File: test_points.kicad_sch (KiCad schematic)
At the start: 17 parts

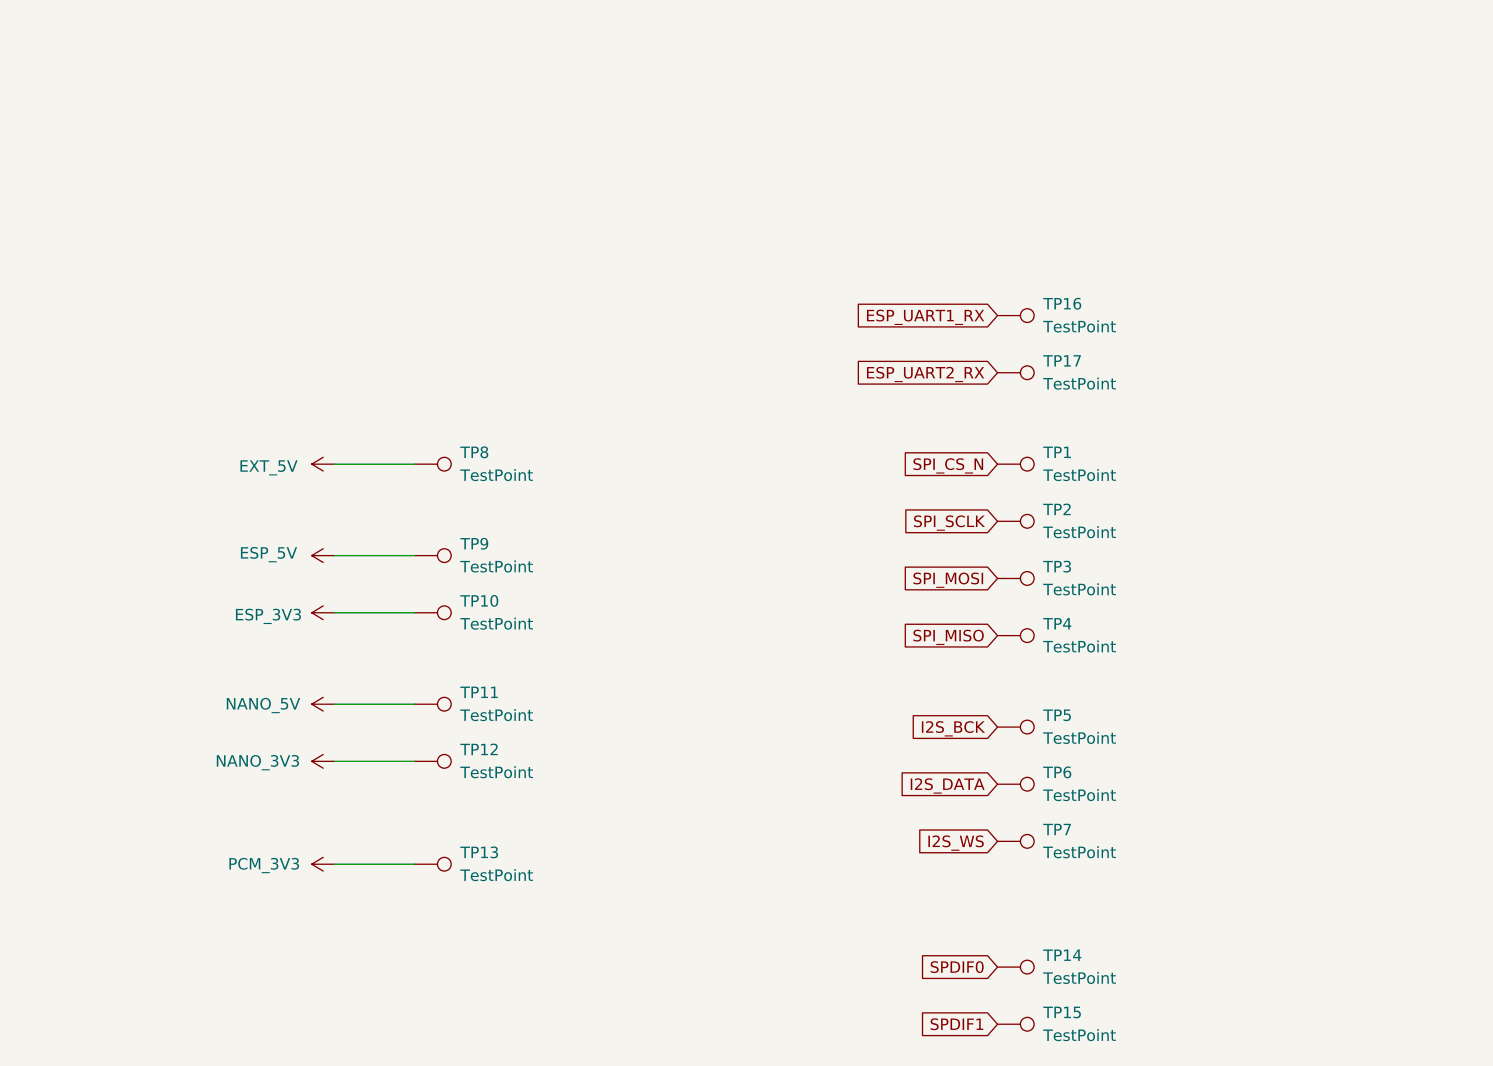
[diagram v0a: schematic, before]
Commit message: Added pin headers for SPI3, I2C0 and I2C1
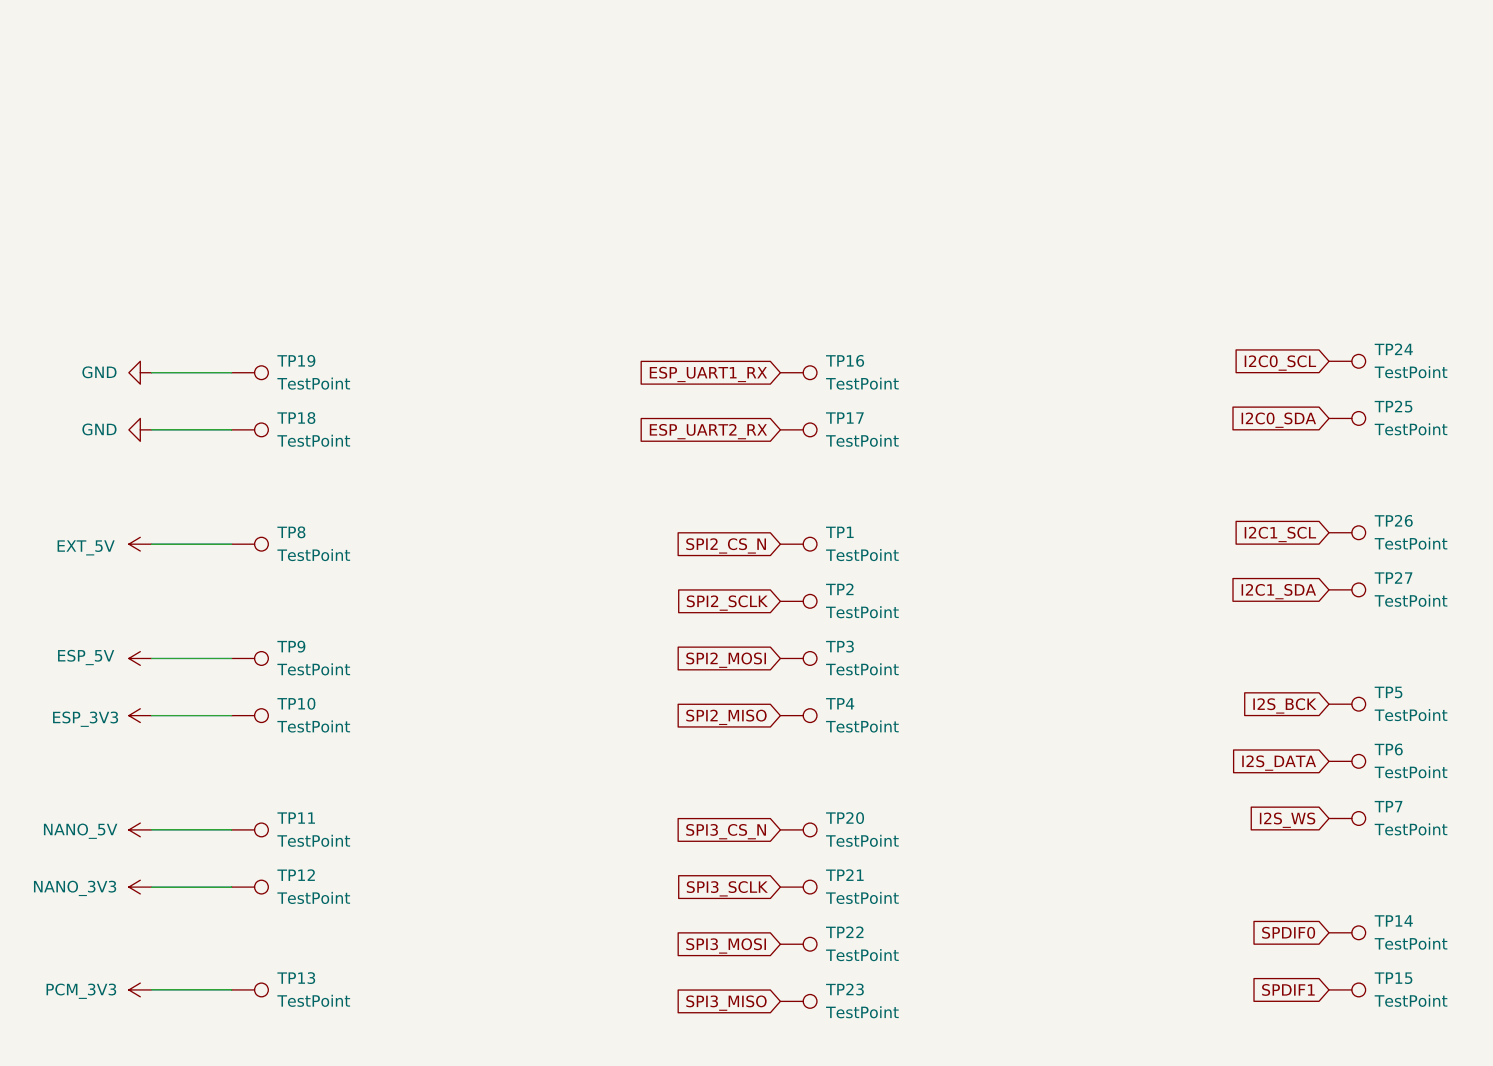
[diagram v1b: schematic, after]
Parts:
- added TP18, TP19, TP20, TP21, TP22, TP23, TP24, TP25, TP26, TP27: TestPoint, symbol Connector:TestPoint
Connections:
- net SPI_CS_N renamed SPI2_CS_N
- net SPI_MISO renamed SPI2_MISO
- net SPI_MOSI renamed SPI2_MOSI
- net SPI_SCLK renamed SPI2_SCLK
- new net GND: TP18.1, TP19.1
- new net I2C0_SCL: TP24.1
- new net I2C0_SDA: TP25.1
- new net I2C1_SCL: TP26.1
- new net I2C1_SDA: TP27.1
- new net SPI3_CS_N: TP20.1
- new net SPI3_MISO: TP23.1
- new net SPI3_MOSI: TP22.1
- new net SPI3_SCLK: TP21.1
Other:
- moved on the sheet: TP1, TP10, TP11, TP12, TP13, TP14, TP15, TP16, TP17, TP2, TP3, TP4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

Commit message: Added jumpers for FM and FIL to DAC. Added pin headers for audio out to DAC. Minor adjustments.
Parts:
- added TP28, TP29: TestPoint, TestPoint:TestPoint_Plated_Hole_D2.0mm, symbol Connector:TestPoint
- TP1, TP10, TP11, TP12, TP13, TP14, TP15, TP16, TP17, TP18, TP19, TP2, TP20, TP21, TP22, TP23, TP24, TP25, TP26, TP27, TP3, TP4, TP5, TP6, TP7, TP8, TP9: footprint (none) -> TestPoint:TestPoint_Plated_Hole_D2.0mm
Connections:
- new net ESP_UART0_RX: TP28.1, TP29.1

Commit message: Completely routed PCB
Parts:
- removed TP17: TestPoint, TestPoint:TestPoint_Plated_Hole_D2.0mm, symbol Connector:TestPoint
- added TP30: TestPoint, TestPoint:TestPoint_Plated_Hole_D2.0mm, symbol Connector:TestPoint
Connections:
- net ESP_UART0_RX: no longer TP29.1
- net ESP_UART2_RX: now also TP30.1
- new net ESP_UART0_TX: TP29.1
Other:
- moved on the sheet: TP16, TP28, TP29
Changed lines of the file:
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@@
 		)
 	)
-	(global_label "ESP_UART0_RX"
+	(global_label "ESP_UART0_TX"
 		(shape input)
-		(at 148.59 52.07 180)
+		(at 148.59 34.29 180)
 		(fields_autoplaced yes)
 		(effects
@@
 		)
 		(property "Intersheetrefs" "${INTERSHEET_REFS}"
-			(at 131.6954 52.07 0)
+			(at 131.6954 34.29 0)
 			(hide yes)
 			(show_name no)
@@
 		)
 	)
-	(global_label "SPI3_MISO"
+	(global_label "ESP_UART2_RX"
 		(shape input)
-		(at 148.59 134.62 180)
+		(at 148.59 64.77 180)
 		(fields_autoplaced yes)
 		(effects
@@
 		)
 		(property "Intersheetrefs" "${INTERSHEET_REFS}"
-			(at 136.9567 134.62 0)
+			(at 131.6954 64.77 0)
 			(hide yes)
 			(show_name no)
@@
 		)
 	)
-	(global_label "SPDIF1"
+	(global_label "SPI3_MISO"
 		(shape input)
-		(at 209.55 133.35 180)
+		(at 148.59 134.62 180)
 		(fields_autoplaced yes)
 		(effects
@@
 		)
 		(property "Intersheetrefs" "${INTERSHEET_REFS}"
-			(at 197.7353 133.35 0)
+			(at 136.9567 134.62 0)
 			(hide yes)
 			(show_name no)
@@
 		)
 	)
-	(global_label "I2C1_SCL"
+	(global_label "SPDIF1"
 		(shape input)
-		(at 209.55 82.55 180)
+		(at 209.55 133.35 180)
 		(fields_autoplaced yes)
 		(effects
@@
 		)
 		(property "Intersheetrefs" "${INTERSHEET_REFS}"
-			(at 198.7634 82.55 0)
+			(at 197.7353 133.35 0)
 			(hide yes)
 			(show_name no)
@@
 		)
 	)
-	(global_label "SPI3_MOSI"
+	(global_label "I2C1_SCL"
 		(shape input)
-		(at 148.59 128.27 180)
+		(at 209.55 82.55 180)
 		(fields_autoplaced yes)
 		(effects
@@
 		)
 		(property "Intersheetrefs" "${INTERSHEET_REFS}"
-			(at 136.9567 128.27 0)
+			(at 198.7634 82.55 0)
 			(hide yes)
 			(show_name no)
@@
 		)
 	)
-	(global_label "ESP_UART1_RX"
+	(global_label "SPI3_MOSI"
 		(shape input)
-		(at 148.59 64.77 180)
+		(at 148.59 128.27 180)
 		(fields_autoplaced yes)
 		(effects
@@
 		)
 		(property "Intersheetrefs" "${INTERSHEET_REFS}"
-			(at 131.6954 64.77 0)
+			(at 136.9567 128.27 0)
 			(hide yes)
 			(show_name no)
@@
 		)
 	)
-	(global_label "SPI2_MISO"
+	(global_label "ESP_UART1_RX"
 		(shape input)
-		(at 148.59 102.87 180)
+		(at 148.59 46.99 180)
 		(fields_autoplaced yes)
 		(effects
@@
 		)
 		(property "Intersheetrefs" "${INTERSHEET_REFS}"
-			(at 136.9567 102.87 0)
+			(at 131.6954 46.99 0)
 			(hide yes)
 			(show_name no)
@@
 		)
 	)
-	(global_label "ESP_UART2_RX"
+	(global_label "SPI2_MISO"
 		(shape input)
-		(at 148.59 71.12 180)
+		(at 148.59 102.87 180)
 		(fields_autoplaced yes)
 		(effects
@@
 		)
 		(property "Intersheetrefs" "${INTERSHEET_REFS}"
-			(at 131.6954 71.12 0)
+			(at 136.9567 102.87 0)
 			(hide yes)
 			(show_name no)
@@
 	(global_label "ESP_UART0_RX"
 		(shape input)
-		(at 148.59 45.72 180)
+		(at 148.59 27.94 180)
 		(fields_autoplaced yes)
 		(effects
@@
 		)
 		(property "Intersheetrefs" "${INTERSHEET_REFS}"
-			(at 131.6954 45.72 0)
+			(at 131.6954 27.94 0)
 			(hide yes)
 			(show_name no)
@@
 	(symbol
 		(lib_id "Connector:TestPoint")
-		(at 148.59 71.12 270)
-		(unit 1)
-		(body_style 1)
-		(exclude_from_sim no)
-		(in_bom yes)
-		(on_board yes)
-		(in_pos_files yes)
-		(dnp no)
-		(fields_autoplaced yes)
-		(property "Reference" "TP17"
-			(at 153.67 69.8499 90)
-			(show_name no)
-			(do_not_autoplace no)
-			(effects
-				(font
-					(size 1.27 1.27)
-				)
-				(justify left)
-			)
-		)
-		(property "Value" "TestPoint"
-			(at 153.67 72.3899 90)
-			(show_name no)
-			(do_not_autoplace no)
-			(effects
-				(font
-					(size 1.27 1.27)
-				)
-				(justify left)
-			)
-		)
-		(property "Footprint" "TestPoint:TestPoint_Plated_Hole_D2.0mm"
-			(at 148.59 76.2 0)
-			(hide yes)
-			(show_name no)
-			(do_not_autoplace no)
-			(effects
-				(font
-					(size 1.27 1.27)
-				)
-			)
-		)
-		(property "Datasheet" ""
-			(at 148.59 76.2 0)
-			(hide yes)
-			(show_name no)
-			(do_not_autoplace no)
-			(effects
-				(font
-					(size 1.27 1.27)
-				)
-			)
-		)
-		(property "Description" "test point"
-			(at 148.59 71.12 0)
-			(hide yes)
-			(show_name no)
-			(do_not_autoplace no)
-			(effects
-				(font
-					(size 1.27 1.27)
-				)
-			)
-		)
-		(pin "1"
-		)
-		(instances
-			(project "noaidi-fpga-synth"
-				(path "/cdb67adb-92dd-404c-89af-7e06e4562fd6"
-					(reference "TP17")
-					(unit 1)
-				)
-			)
-		)
-	)
-	(symbol
-		(lib_id "Connector:TestPoint")
 		(at 148.59 83.82 270)
 		(unit 1)
@@
 	(symbol
 		(lib_id "Connector:TestPoint")
-		(at 148.59 64.77 270)
+		(at 148.59 46.99 270)
 		(unit 1)
 		(body_style 1)
@@
 		(fields_autoplaced yes)
 		(property "Reference" "TP16"
-			(at 153.67 63.4999 90)
+			(at 153.67 45.7199 90)
 			(show_name no)
 			(do_not_autoplace no)
@@
 		)
 		(property "Value" "TestPoint"
-			(at 153.67 66.0399 90)
+			(at 153.67 48.2599 90)
+			(hide yes)
 			(show_name no)
 			(do_not_autoplace no)
@@
 		)
 		(property "Footprint" "TestPoint:TestPoint_Plated_Hole_D2.0mm"
-			(at 148.59 69.85 0)
+			(at 148.59 52.07 0)
 			(hide yes)
 			(show_name no)
@@
 		)
 		(property "Datasheet" ""
-			(at 148.59 69.85 0)
+			(at 148.59 52.07 0)
 			(hide yes)
 			(show_name no)
@@
 		)
 		(property "Description" "test point"
-			(at 148.59 64.77 0)
+			(at 148.59 46.99 0)
 			(hide yes)
 			(show_name no)
@@
 	(symbol
 		(lib_id "Connector:TestPoint")
-		(at 148.59 52.07 270)
+		(at 148.59 34.29 270)
 		(unit 1)
 		(body_style 1)
@@
 		(fields_autoplaced yes)
 		(property "Reference" "TP29"
-			(at 153.67 50.7999 90)
+			(at 153.67 33.0199 90)
 			(show_name no)
 			(do_not_autoplace no)
@@
 		)
 		(property "Value" "TestPoint"
-			(at 153.67 53.3399 90)
+			(at 153.67 35.5599 90)
 			(show_name no)
 			(do_not_autoplace no)
@@
 		)
 		(property "Footprint" "TestPoint:TestPoint_Plated_Hole_D2.0mm"
-			(at 148.59 57.15 0)
+			(at 148.59 39.37 0)
 			(hide yes)
 			(show_name no)
@@
 		)
 		(property "Datasheet" ""
-			(at 148.59 57.15 0)
+			(at 148.59 39.37 0)
 			(hide yes)
 			(show_name no)
@@
 		)
 		(property "Description" "test point"
-			(at 148.59 52.07 0)
+			(at 148.59 34.29 0)
 			(hide yes)
 			(show_name no)
@@
 	(symbol
 		(lib_id "Connector:TestPoint")
-		(at 148.59 45.72 270)
+		(at 148.59 27.94 270)
 		(unit 1)
 		(body_style 1)
@@
 		(fields_autoplaced yes)
 		(property "Reference" "TP28"
-			(at 153.67 44.4499 90)
+			(at 153.67 26.6699 90)
 			(show_name no)
 			(do_not_autoplace no)
@@
 		)
 		(property "Value" "TestPoint"
-			(at 153.67 46.9899 90)
+			(at 153.67 29.2099 90)
 			(show_name no)
 			(do_not_autoplace no)
@@
 		)
 		(property "Footprint" "TestPoint:TestPoint_Plated_Hole_D2.0mm"
-			(at 148.59 50.8 0)
+			(at 148.59 33.02 0)
 			(hide yes)
 			(show_name no)
@@
 		)
 		(property "Datasheet" ""
-			(at 148.59 50.8 0)
+			(at 148.59 33.02 0)
 			(hide yes)
 			(show_name no)
@@
 		)
 		(property "Description" "test point"
-			(at 148.59 45.72 0)
+			(at 148.59 27.94 0)
 			(hide yes)
 			(show_name no)
@@
 					(unit 1)
 				)
+			)
+		)
+	)
+	(symbol
+		(lib_id "Connector:TestPoint")
+		(at 148.59 64.77 270)
+		(unit 1)
+		(body_style 1)
+		(exclude_from_sim no)
+		(in_bom yes)
+		(on_board yes)
+		(in_pos_files yes)
+		(dnp no)
+		(fields_autoplaced yes)
+		(property "Reference" "TP30"
+			(at 153.67 63.4999 90)
+			(show_name no)
+			(do_not_autoplace no)
+			(effects
+				(font
+					(size 1.27 1.27)
+				)
+				(justify left)
+			)
+		)
+		(property "Value" "TestPoint"
+			(at 153.67 66.0399 90)
+			(show_name no)
+			(do_not_autoplace no)
+			(effects
+				(font
+					(size 1.27 1.27)
+				)
+				(justify left)
+			)
+		)
+		(property "Footprint" "TestPoint:TestPoint_Plated_Hole_D2.0mm"
+			(at 148.59 69.85 0)
+			(hide yes)
+			(show_name no)
+			(do_not_autoplace no)
+			(effects
+				(font
+					(size 1.27 1.27)
+				)
+			)
+		)
+		(property "Datasheet" ""
+			(at 148.59 69.85 0)
+			(hide yes)
+			(show_name no)
+			(do_not_autoplace no)
+			(effects
+				(font
+					(size 1.27 1.27)
+				)
+			)
+		)
+		(property "Description" "test point"
+			(at 148.59 64.77 0)
+			(hide yes)
+			(show_name no)
+			(do_not_autoplace no)
+			(effects
+				(font
+					(size 1.27 1.27)
+				)
+			)
+		)
+		(pin "1"
+		)
+		(instances
+			(project "noaidi-fpga-synth"
+				(path "/cdb67adb-92dd-404c-89af-7e06e4562fd6"
+					(reference "TP30")
+					(unit 1)
+				)
